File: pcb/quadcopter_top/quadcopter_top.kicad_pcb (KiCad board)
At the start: 2 copper layers, 48.3 x 73.7 mm, 12 parts, among them IC1 ATMEGA328P-A, J1 RJ45

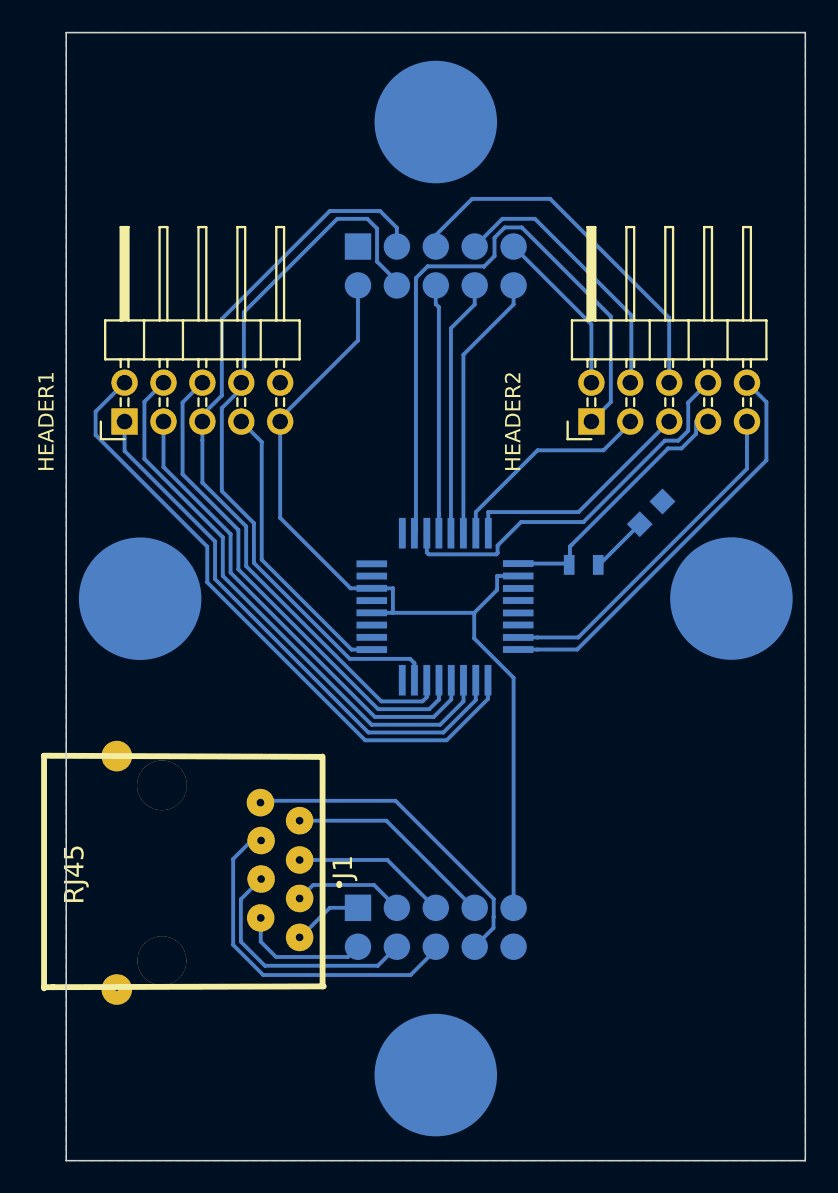
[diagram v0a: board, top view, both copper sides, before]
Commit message: Added cal poly logo and set up backside
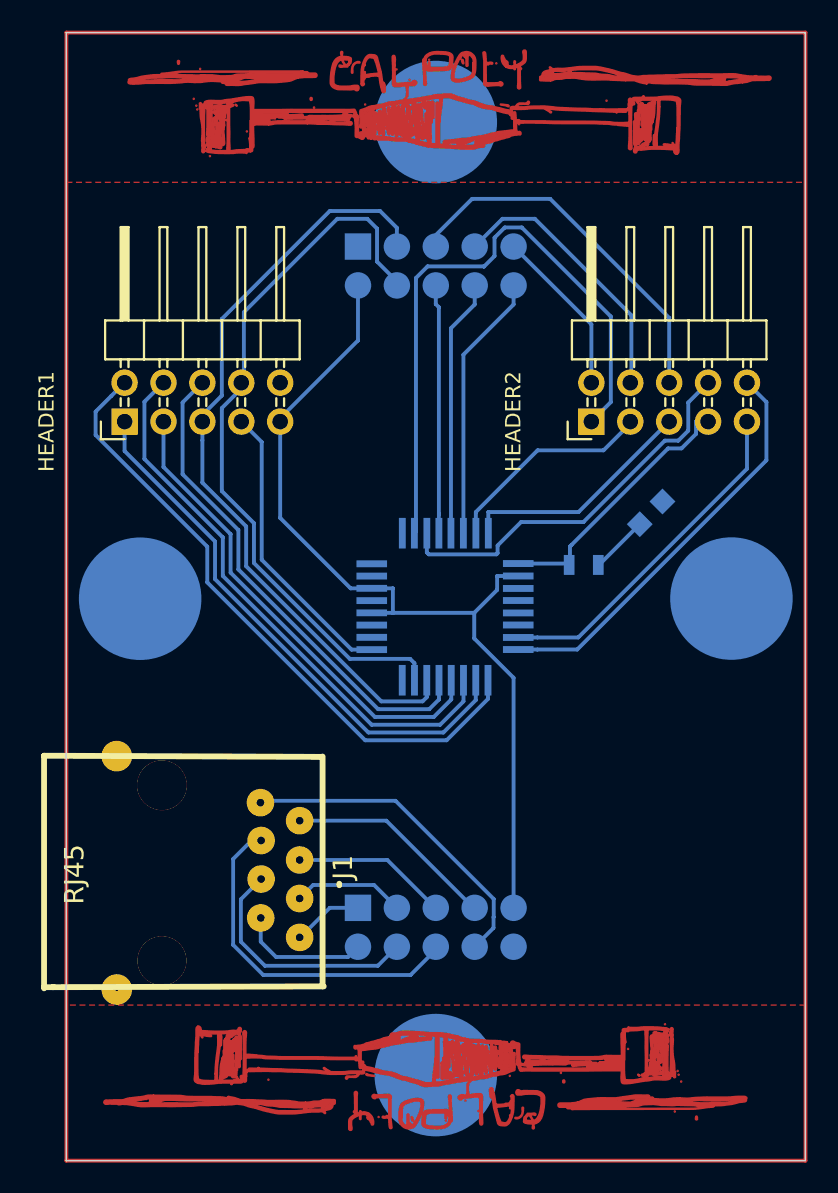
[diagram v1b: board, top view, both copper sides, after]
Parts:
- added G***: LOGO, quadcopter_footprints:logo_mirror, F.Cu at (223.9, 116.8)
- added G***: LOGO, quadcopter_footprints:logo_mirror, F.Cu at (225.2, 55.1)
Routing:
- net (no net): track 0.00 -> 243.8 mm
- added copper zone on F.Cu, net GND
